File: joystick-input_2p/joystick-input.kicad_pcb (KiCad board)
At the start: 2 copper layers, 53.3 x 39.9 mm, 16 parts, among them J1 Conn_01x18, J2 Conn_02x14_Odd_Even

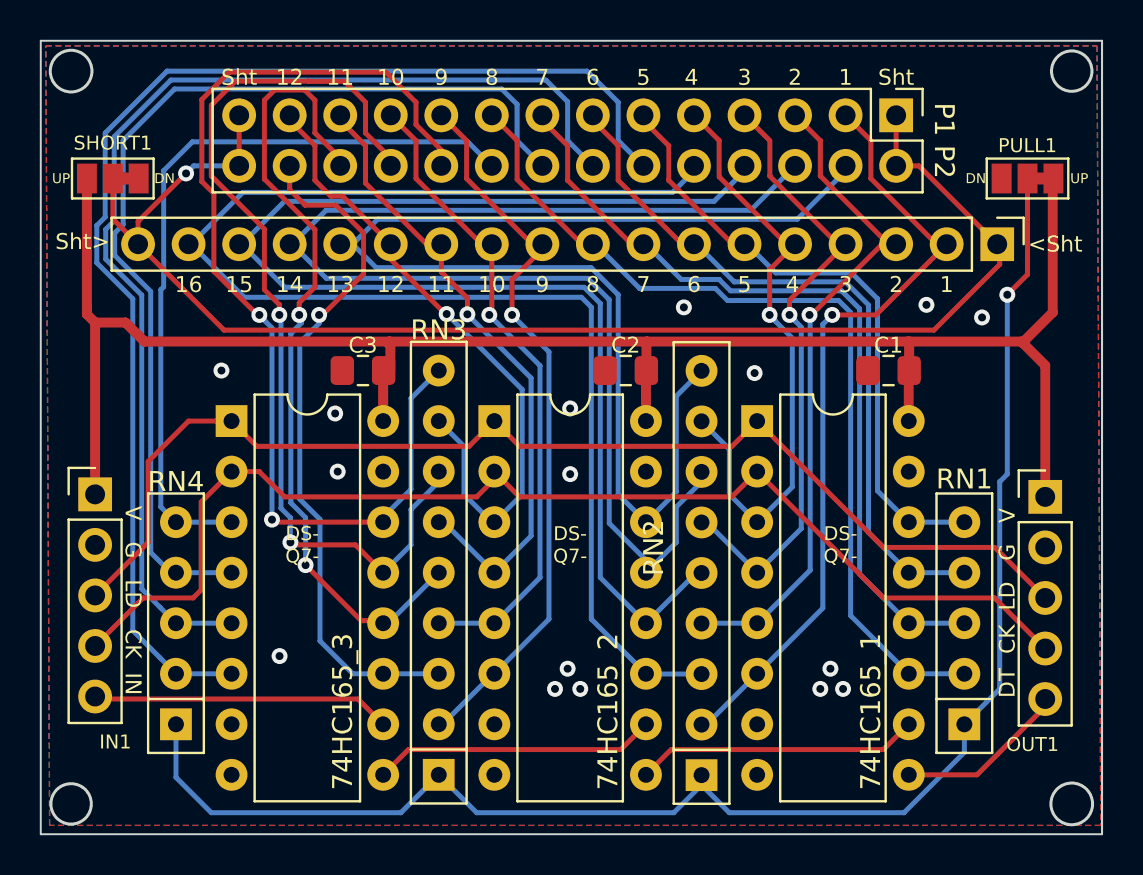
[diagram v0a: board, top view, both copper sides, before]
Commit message: joystick-input_2p 스크린샷
Signed-off-by: Ju, Gyeong-min <jcmh74@gmail.com>
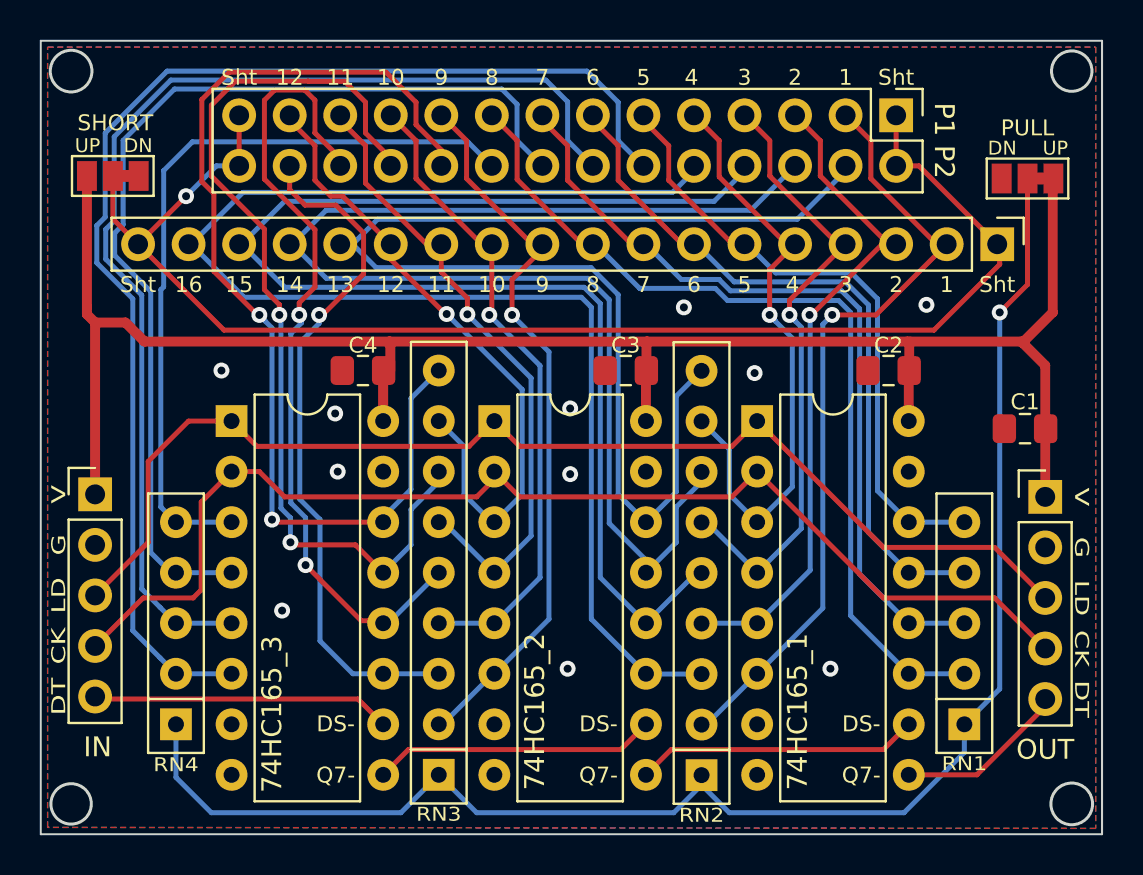
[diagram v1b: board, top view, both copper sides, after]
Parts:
- added C1: C, Capacitor_SMD:C_0805_2012Metric_Pad1.18x1.45mm_HandSolder, F.Cu at (161.3, 87.2)
- moved SHORT1 0.13 mm to (115.4, 74.5)
- renumbered C1 to C2, C2 to C3, C3 to C4
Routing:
- net /C_SHORT: track 70.5 -> 69.8 mm
- net /C_P1_DOWN: track 35.0 -> 34.5 mm
- net /C_P2_L: track 41.6 -> 41.1 mm
- net GND: vias 16 -> 11
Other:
- board text added: "CK"
- board text added: "DT"
- board text added: "G"
- board text added: "IN"
- board text added: "LD"
- board text added: "OUT"
- board text added: "PULL"
- board text added: "Rev.3"
- board text added: "SHORT"
- board text added: "V"
- board text removed: "<Sht"
- board text removed: "DT CK LD G V"
- board text removed: "Rev.2"
- board text removed: "Sht>"
- board text removed: "V G LD CK IN"

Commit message: joystick_input 레이아웃 변경
Signed-off-by: Ju, Gyeong-min <jcmh74@gmail.com>
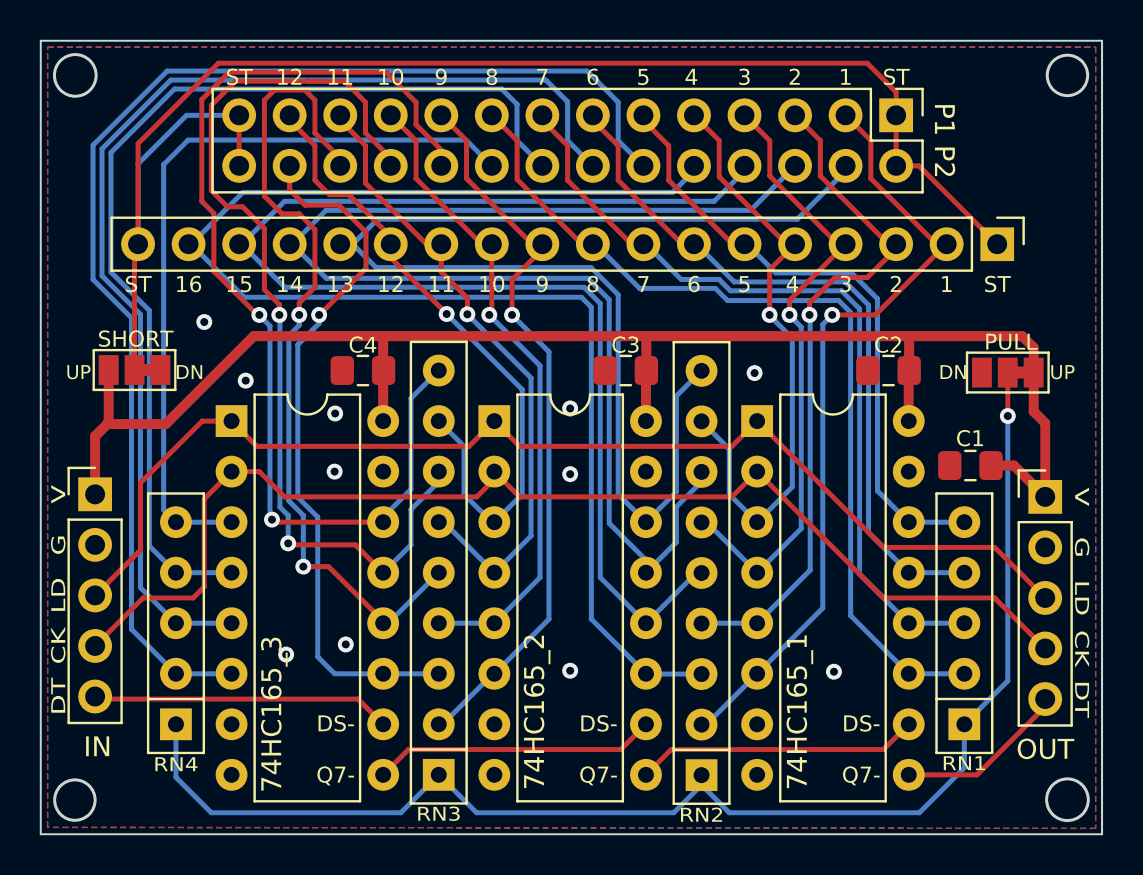
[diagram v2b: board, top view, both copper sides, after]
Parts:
- moved SHORT1 9.81 mm to (116.5, 84.3)
- moved PULL1 9.80 mm to (160.4, 84.4)
- moved C1 3.31 mm to (158.5, 89.1)
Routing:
- net VCC: track 92.3 -> 79.8 mm
- net /PULL: track 77.2 -> 67.5 mm
- net /C_SHORT: track 69.8 -> 74.9 mm, vias 1 -> 0
- net /C_P1_DOWN: track 34.5 -> 35.4 mm
- net /C_P2_R: track 34.8 -> 35.5 mm
- net /C_P2_L: track 41.1 -> 41.7 mm
- net /C_P2_Y: track 47.6 -> 48.1 mm
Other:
- outline, holes or cut-outs redrawn
- board text added: "ST"
- board text removed: "Sht"

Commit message: 74hc165 board array-resistance change
Signed-off-by: Ju, Gyeong-min <jcmh74@gmail.com>
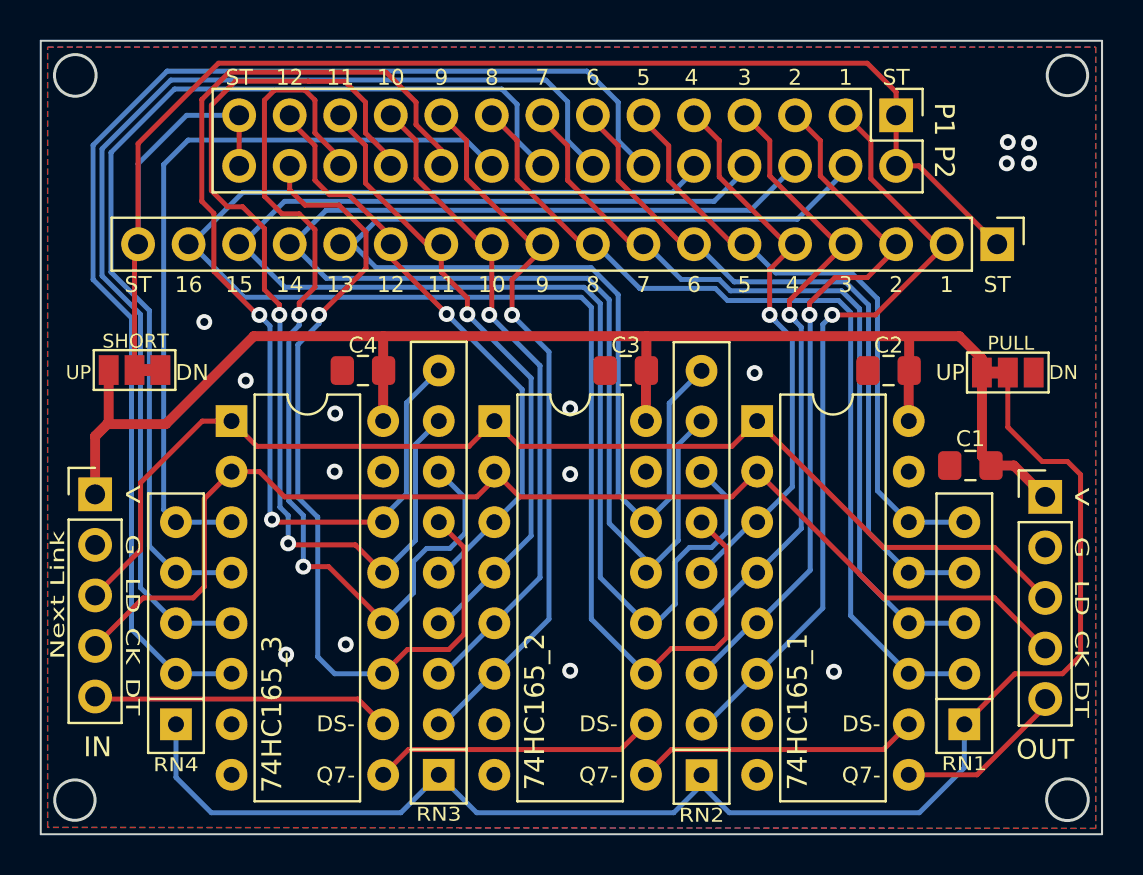
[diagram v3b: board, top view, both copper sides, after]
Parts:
- turned PULL1 to 0 degrees
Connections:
- RN2 pad 3: /C_P2_RIGHT -> /C_P1_DOWN
- RN2 pad 4: /C_P1_DOWN -> /C_P1_LEFT
- RN2 pad 5: /C_P2_LEFT -> /C_P1_RIGHT
- RN2 pad 6: /C_P1_LEFT -> /C_P2_RIGHT
- RN2 pad 7: /C_P2_DOWN -> /C_P2_LEFT
- RN2 pad 8: /C_P1_RIGHT -> /C_P2_DOWN
- RN3 pad 3: /C_P2_R -> /C_P1_Y
- RN3 pad 4: /C_P1_Y -> /C_P1_L
- RN3 pad 5: /C_P2_L -> /C_P1_R
- RN3 pad 6: /C_P1_L -> /C_P2_R
- RN3 pad 7: /C_P2_Y -> /C_P2_L
- RN3 pad 8: /C_P1_R -> /C_P2_Y
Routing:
- net /C_P2_RIGHT: track 70.6 -> 78.9 mm
- net /C_P2_R: track 35.5 -> 43.8 mm
- net /C_P2_LEFT: track 66.9 -> 73.8 mm
- net /C_P2_L: track 41.7 -> 48.4 mm
- net /PULL: track 67.5 -> 72.6 mm, vias 1 -> 0
- net VCC: track 79.8 -> 75.3 mm
- net /C_P2_DOWN: track 64.2 -> 67.2 mm
- net /C_P2_Y: track 48.1 -> 50.6 mm
- net /C_P1_R: track 32.5 -> 30.0 mm
- net /C_P1_RIGHT: track 30.8 -> 28.4 mm
- net /C_P1_DOWN: track 35.4 -> 36.5 mm
- net /C_P1_Y: track 32.8 -> 33.8 mm
- net GND: vias 11 -> 15
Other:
- board text added: "Next Link"
- board text added: "Rev.4"
- board text removed: "Rev.3"
